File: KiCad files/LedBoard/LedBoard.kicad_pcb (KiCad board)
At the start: 2 copper layers, 40 x 40 mm, 19 parts, among them J1 Conn_01x02, SW1 SW_SPST, U1 TPS565208

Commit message: updated LED board
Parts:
- removed C6: 22uF 0805, Capacitor_SMD:C_0805_2012Metric
- removed LED4: KW H3L531.TE, KW_H3L531.TE:KW_H3L531.TE
- removed U1: TPS565208, Package_TO_SOT_SMD:SOT-23-6
- added PS1: TPS566242DRLR, Package_TO_SOT_SMD:SOT-563, F.Cu at (79.8, 47.2)
- added R3: 23.2K 0805, Resistor_SMD:R_0805_2012Metric, F.Cu at (79.9, 43.0)
- added R4: 30K 0805, Resistor_SMD:R_0805_2012Metric, F.Cu at (84.8, 43.0)
- C1: value 10uF 0805 -> 100nF
- C3: value 10uF 0805 -> 100nF 0805
- C4: value 0.1uF 0805 -> 22uF
- C5: value 22uF 0805 -> 100nF
- L1: value 2.2uH 10A -> MDA7030-2R2M; footprint Inductor_SMD:L_Sunlord_MWSA0624S -> Inductor_SMD:L_Coilcraft_XAL7030-222
- LED1, LED2, LED3: value KW H3L531.TE -> GW_VJLPL1.CM-K3LX-XX51-1; footprint KW_H3L531.TE:KW_H3L531.TE -> GWVJLPL1CMK3LXXX511:GWVJLPL1CMK3LXXX511
- R1: value Value: 10K 0805 -> 100K 0805
- R2: value 190mΩ 2512 -> 120K 0805; footprint Resistor_SMD:R_2512_6332Metric -> Resistor_SMD:R_0805_2012Metric
- moved C4 17.1 mm to (97.3, 50.5), turned to -90 degrees
- moved R2 13.7 mm to (83.4, 44.5), turned to 135 degrees
- moved LED2 11.1 mm to (98.5, 37.0), turned to -90 degrees
- moved C5 7.22 mm to (95.3, 50.5), turned to -90 degrees
- moved LED1 6.85 mm to (81.5, 37.0), turned to -90 degrees
- moved R1 6.51 mm to (78.5, 45.4), turned to -135 degrees
- moved C1 6.13 mm to (82.0, 45.9), turned to 135 degrees
- moved C3 4.32 mm to (75.8, 45.2), turned to 45 degrees
- moved LED3 3.44 mm to (90.0, 37.0), turned to -90 degrees
- moved L1 2.88 mm to (90.0, 49.6)
- moved C2 0.40 mm to (77.9, 48.7), turned to -45 degrees
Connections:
- net +12V renamed VCC
- C1 pad 1: Net-(U1-VBST) -> LED_V+
- C1 pad 2: Net-(U1-SW) -> Net-(PS1-FB)
- C2 pad 1: Net-(SW1-A) -> Net-(PS1-VIN)
- C3 pad 1: Net-(SW1-A) -> Net-(PS1-VIN)
- C4 pad 1: Net-(SW1-A) -> LED_V+
- C5 pad 1: Net-(C5-Pad1) -> LED_V+
- L1 pad 1: Net-(U1-SW) -> Net-(PS1-SW)
- L1 pad 2: Net-(C5-Pad1) -> LED_V+
- LED1 pad 1: Net-(C5-Pad1) -> GND
- LED1 pad 2: Net-(C5-Pad1) -> LED_V+
- LED2 pad 1: Net-(C5-Pad1) -> GND
- LED2 pad 2: Net-(C5-Pad1) -> LED_V+
- LED3 pad 1: Net-(C5-Pad1) -> GND
- LED3 pad 2: Net-(C5-Pad1) -> LED_V+
- R1 pad 2: Net-(SW1-A) -> Net-(PS1-VIN)
- R2 pad 1: Net-(U1-VFB) -> LED_V+
- R2 pad 2: GND -> Net-(PS1-FB)
- SW1 pad 1: Net-(SW1-A) -> Net-(PS1-VIN)
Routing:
- net Net-(U1-VFB): track 98.6 -> 0.00 mm
- net LED_V+: track 0.00 -> 72.6 mm
- net Net-(C5-Pad1): track 46.8 -> 0.00 mm
- net Net-(SW1-A): track 20.6 -> 0.00 mm
- net Net-(PS1-VIN): track 0.00 -> 12.7 mm
- net Net-(PS1-SW): track 0.00 -> 12.0 mm
- net Net-(U1-SW): track 8.06 -> 0.00 mm
- net GND: track 1.85 -> 7.86 mm
- net Net-(PS1-FB): track 0.00 -> 5.80 mm
- net Net-(PS1-EN): track 2.58 -> 5.08 mm
- net Net-(U1-VBST): track 2.09 -> 0.00 mm

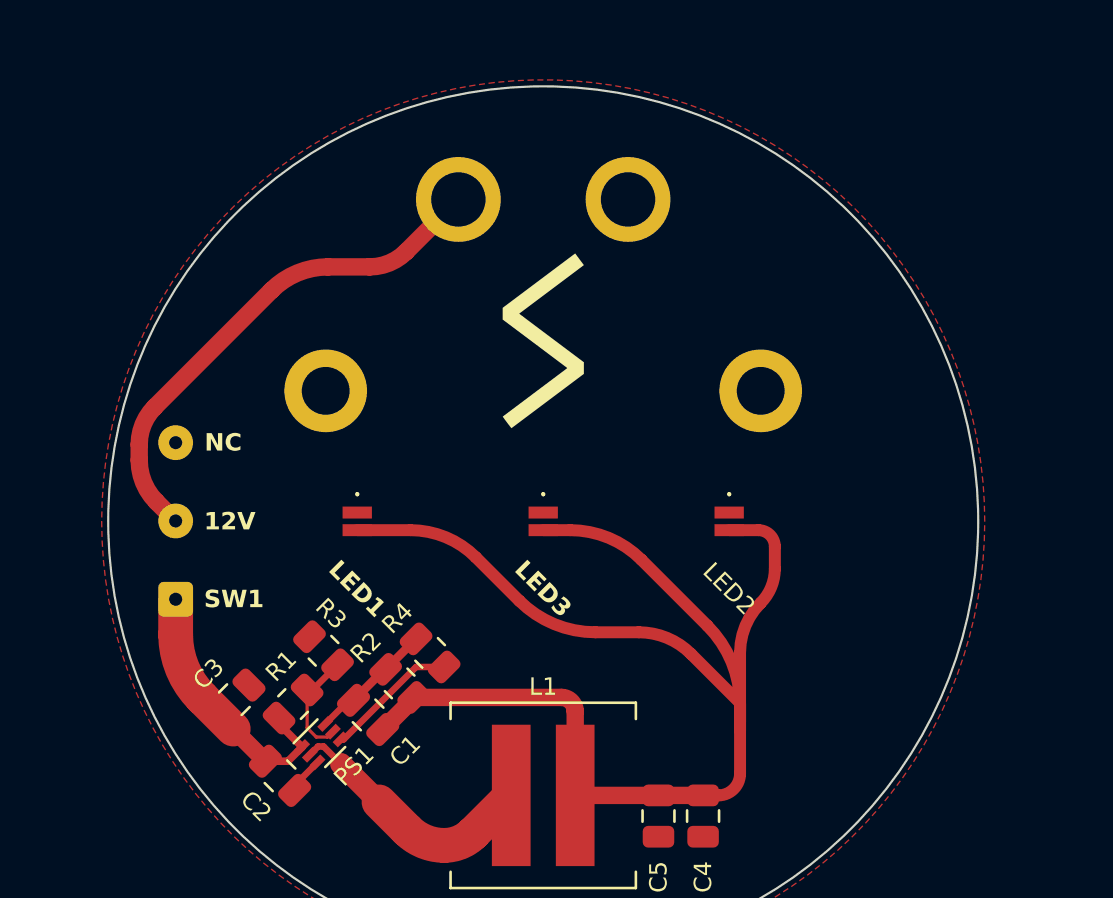
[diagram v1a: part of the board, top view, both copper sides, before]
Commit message: added giant npn mosfet on led board, needs to be removed from controller board
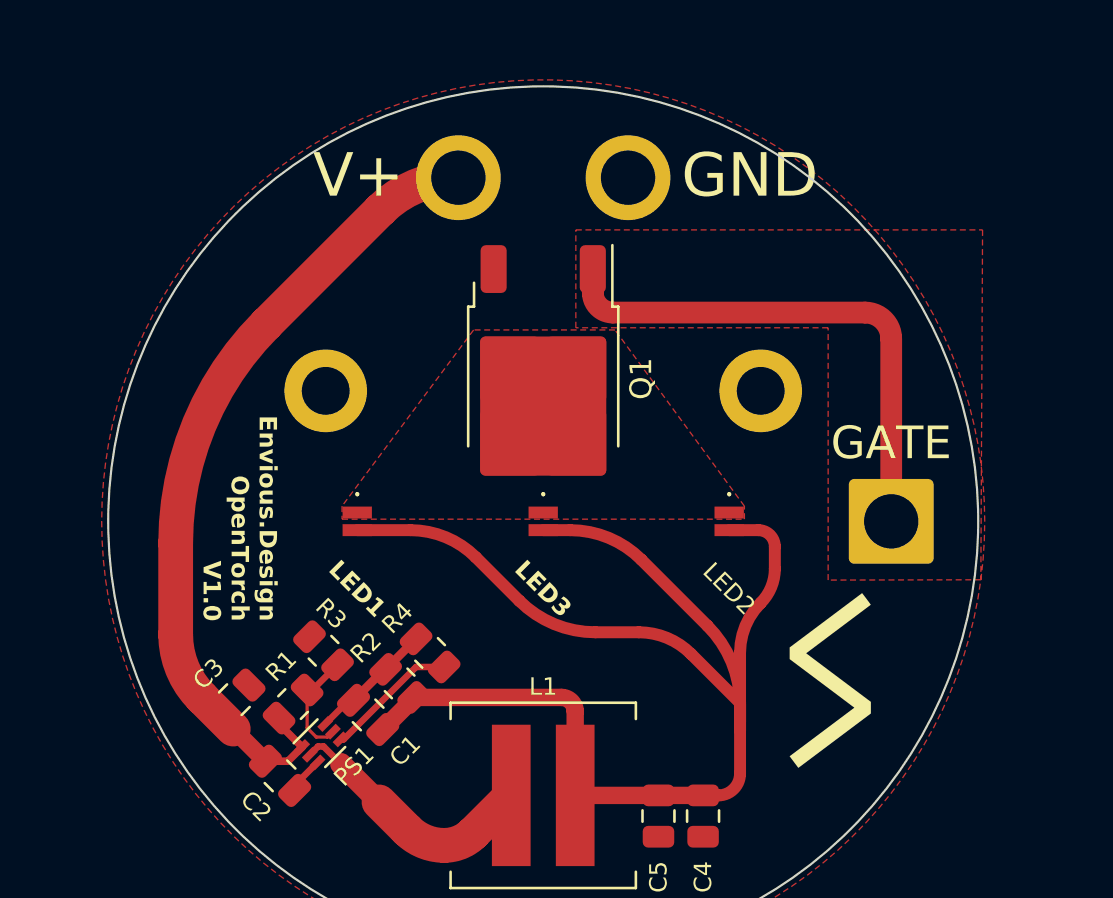
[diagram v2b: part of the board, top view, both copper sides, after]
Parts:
- removed SW1: SW_SPST, Connector_Wire:SolderWire-0.1sqmm_1x03_P3.6mm_D0.4mm_OD1mm
- added J2: Conn_01x02, Connector_Wire:SolderWire-2sqmm_1x01_D2mm_OD3.9mm, F.Cu at (106.0, 37.0)
- added Q1: IRLR120NTRPBF, Package_TO_SOT_SMD:TO-252-2, F.Cu at (90.0, 30.4)
- moved G*** 20.6 mm to (103.2, 44.4), turned to 180 degrees
- moved J1 1.00 mm to (86.1, 21.2)
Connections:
- C2 pad 1: Net-(PS1-VIN) -> VCC
- C3 pad 1: Net-(PS1-VIN) -> VCC
- LED1 pad 1: GND -> Net-(Q1-D)
- LED2 pad 1: GND -> Net-(Q1-D)
- LED3 pad 1: GND -> Net-(Q1-D)
- PS1 pad 1: Net-(PS1-VIN) -> VCC
- R1 pad 2: Net-(PS1-VIN) -> VCC
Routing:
- net Net-(J2-Pin_1): track 0.00 -> 24.3 mm
- net VCC: track 23.6 -> 37.8 mm
- net Net-(PS1-VIN): track 12.7 -> 0.00 mm
- added copper zone on F.Cu, net Net-(J2-Pin_1)
- added copper zone on F.Cu, net Net-(Q1-D)
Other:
- board text added: "GATE"
- board text added: "GND"
- board text added: "V+"
- board text removed: "12V"
- board text removed: "NC"
- board text removed: "SW1"

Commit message: made some small tweaks
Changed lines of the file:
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@@
     (property "ki_description" "LED Lighting OSLON Pure 1414 White, Cool 6500K 2.8V 350mA 120 0505 (1313 Metric)")
     (attr smd)
-    (fp_text reference "LED2" (at 3.1 0 -225) (layer "F.SilkS")
+    (fp_text reference "LED2" (at -2.5 0 -180) (layer "F.SilkS")
         (effects (font (size 0.8 0.8) (thickness 0.153)))
     )
@@
     (property "ki_description" "LED Lighting OSLON Pure 1414 White, Cool 6500K 2.8V 350mA 120 0505 (1313 Metric)")
     (attr smd)
-    (fp_text reference "LED3" (at 3.1 0 -225) (layer "F.SilkS")
+    (fp_text reference "LED3" (at 2.25 0) (layer "F.SilkS")
         (effects (font (size 0.8 0.8) (thickness 0.153) bold))
     )
@@
     (property "ki_description" "LED Lighting OSLON Pure 1414 White, Cool 6500K 2.8V 350mA 120 0505 (1313 Metric)")
     (attr smd)
-    (fp_text reference "LED1" (at 3.1 0 -225) (layer "F.SilkS")
+    (fp_text reference "LED1" (at -2.25 0 -180) (layer "F.SilkS")
         (effects (font (size 0.8 0.8) (thickness 0.153) bold))
     )
@@
   (gr_circle (center 90 37) (end 110 37)
     (stroke (width 0.1) (type default)) (fill none) (layer "Edge.Cuts"))
-  (gr_text "V+" (at 81.5 21.1) (layer "F.SilkS")
+  (gr_text "V+" (at 81.5 22.75) (layer "F.SilkS")
     (effects (font (size 2 2) (thickness 0.25)))
   )
@@
     (effects (font (size 1.5 1.5) (thickness 0.25)))
   )
-  (gr_text "GND" (at 99.5 21.1) (layer "F.SilkS")
+  (gr_text "GND" (at 99.5 22.75) (layer "F.SilkS")
     (effects (font (size 2 2) (thickness 0.25)))
   )

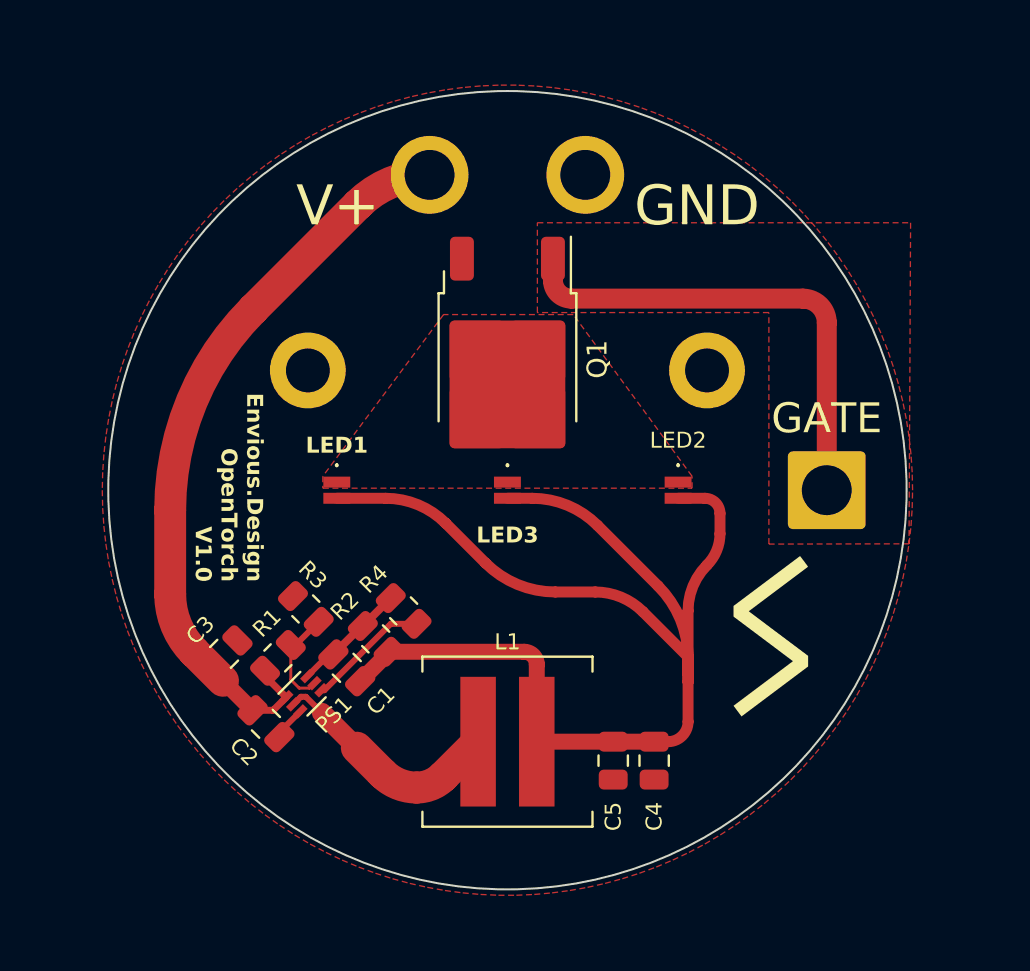
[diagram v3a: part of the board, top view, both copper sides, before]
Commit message: modified IO board and LED board so they connect together using XT60
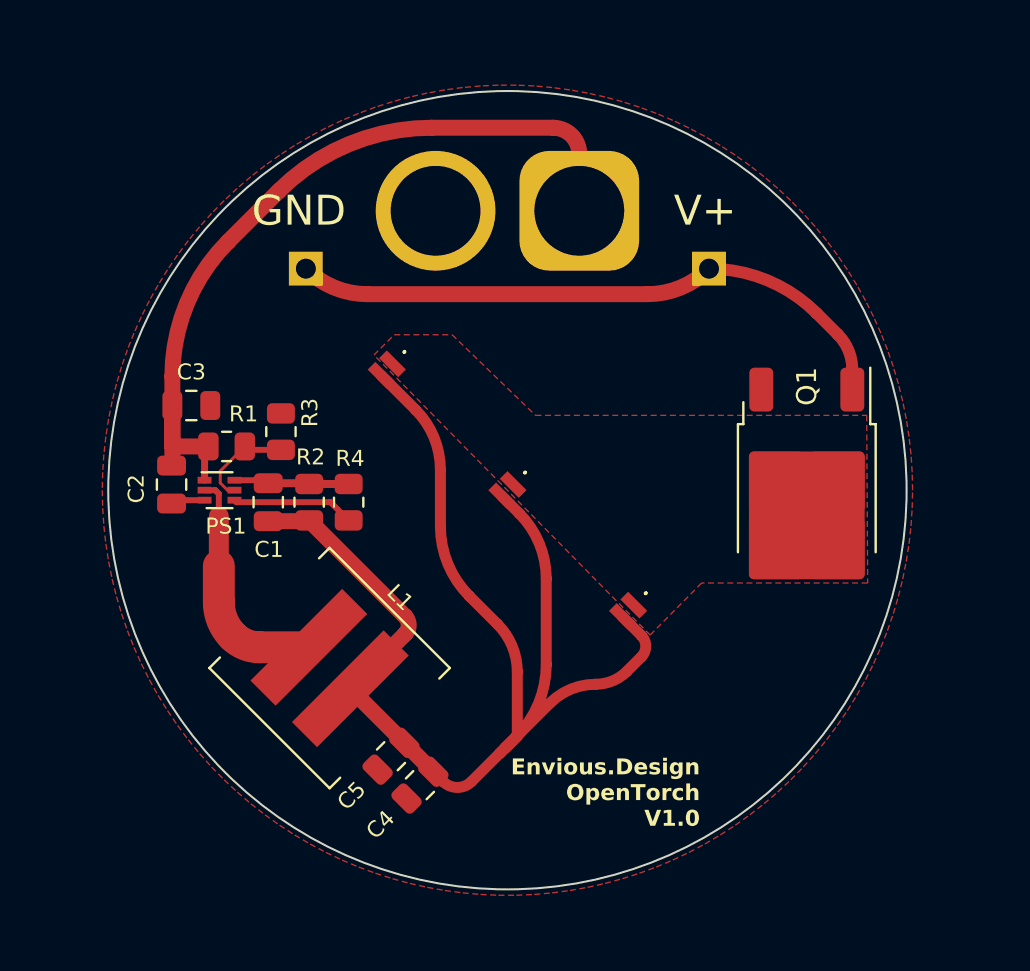
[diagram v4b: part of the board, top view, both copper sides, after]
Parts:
- removed G***: LOGO, GW_CSSRM3:Sun
- removed H1, H2: MountingHole, MountingHole:MountingHole_2.2mm_M2_DIN965_Pad
- added J3: Conn_01x02, Connector_PinSocket_2.54mm:PinSocket_1x01_P2.54mm_Vertical, B.Cu at (79.9, 25.9)
- J1: footprint Connector_Wire:SolderWire-2sqmm_1x02_P7.8mm_D2mm_OD3.9mm -> Connector_AMASS:AMASS_XT60-F_1x02_P7.20mm_Vertical; moved to B.Cu
- J2: footprint Connector_Wire:SolderWire-2sqmm_1x01_D2mm_OD3.9mm -> Connector_PinSocket_2.54mm:PinSocket_1x01_P2.54mm_Vertical; moved to B.Cu
- LED1, LED2, LED3: value GW_VJLPL1.CM-K3LX-XX51-1 -> GW VJLPL1.CM-K3LX-XX55-1
- moved Q1 16.4 mm to (105.0, 37.0)
- moved C2 12.9 mm to (73.2, 36.7), turned to -90 degrees
- moved J2 12.6 mm to (100.1, 25.9), turned to -90 degrees
- moved C3 12.6 mm to (74.2, 32.8), turned to 0 degrees
- moved C4 11.8 mm to (85.6, 51.8), turned to -135 degrees
- moved C5 11.1 mm to (84.2, 50.3), turned to -135 degrees
- moved PS1 11.0 mm to (75.6, 37.0), turned to 0 degrees
- moved R1 10.9 mm to (75.9, 34.8), turned to 180 degrees
- moved L1 9.64 mm to (81.1, 45.9), turned to -45 degrees
- moved C1 9.18 mm to (78.0, 37.6), turned to 90 degrees
- moved R3 8.97 mm to (78.7, 34.1), turned to 90 degrees
- moved J1 7.71 mm to (93.6, 23.0), turned to 180 degrees
- moved R2 7.62 mm to (80.1, 37.6), turned to 90 degrees
- moved LED1 6.54 mm to (84.0, 31.0), turned to -135 degrees
- moved LED2 6.54 mm to (96.0, 43.0), turned to -135 degrees
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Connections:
- net Net-(Q1-D) renamed NPN_DRAIN
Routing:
- net Net-(J2-Pin_1): track 24.3 -> 31.2 mm
- net VCC: track 37.8 -> 40.6 mm
- removed copper zone on F.Cu, net Net-(J2-Pin_1)
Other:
- board text removed: "GATE"
